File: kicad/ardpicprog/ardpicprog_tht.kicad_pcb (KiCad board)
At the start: 2 copper layers, 69.1 x 53.9 mm, 36 parts, among them P1 CONN_01X06, P2 CONN_01X02, Q1 BC548, SW1 SW_PUSH, U1 PIC16F627, U2 MC34063, U3 LM78L12ACZ

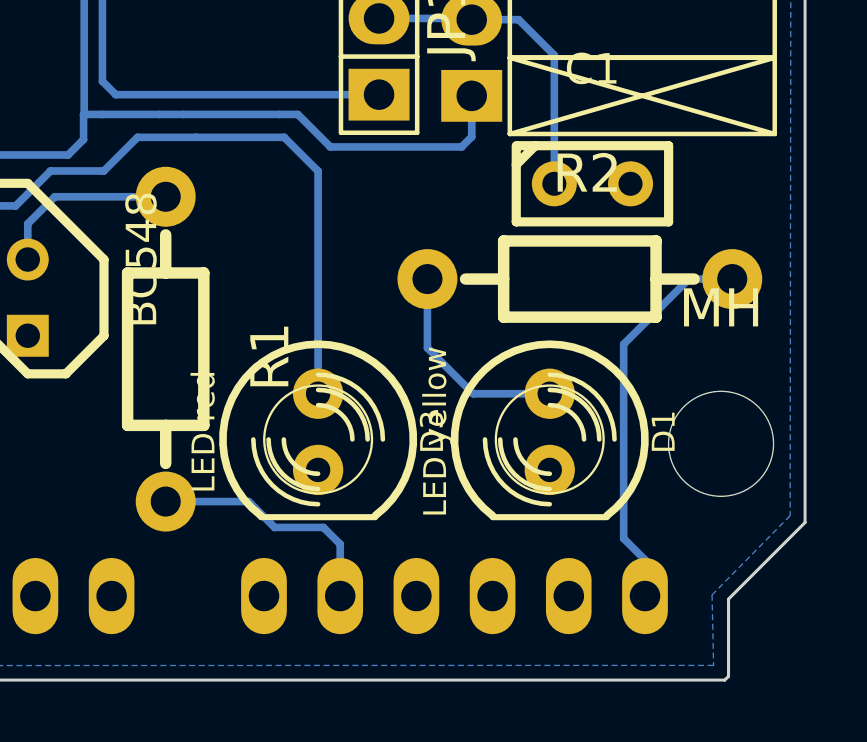
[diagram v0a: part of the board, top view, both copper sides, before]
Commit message: VDD d2 connection fix
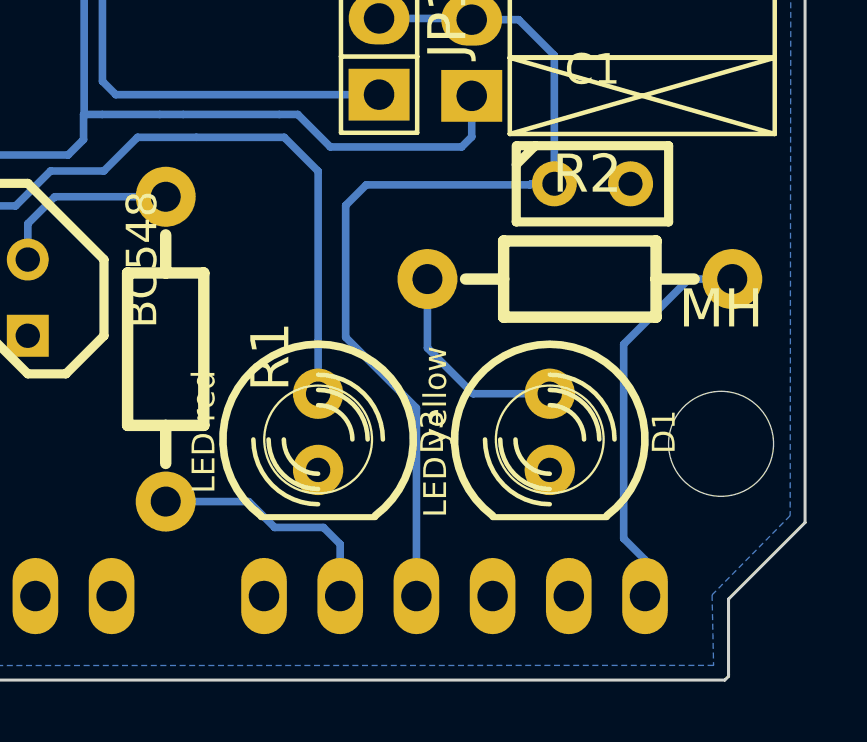
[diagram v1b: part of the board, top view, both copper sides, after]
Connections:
- SHIELD1 pad AD2: (no net) -> VDD(D2)
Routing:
- net VDD(D2): track 10.6 -> 31.9 mm
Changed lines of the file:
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@@
-(kicad_pcb (version 4) (host pcbnew "(2014-jul-16 BZR unknown)-product")
+(kicad_pcb (version 4) (host pcbnew 0.201506232253+5814~23~ubuntu14.04.1-product)
   (general
-    (links 69)
+    (links 70)
     (no_connects 0)
-    (area 76.76617 112.4864 180.28383 175.34946)
+    (area 88.224999 117.774999 157.400001 171.725001)
     (thickness 1.6)
     (drawings 12)
-    (tracks 248)
+    (tracks 255)
     (zones 0)
     (modules 36)
@@
     (pad AD1 thru_hole oval (at 53.34 -2.54 90) (size 2.54 1.524) (drill 1.016) (layers *.Cu *.Mask F.SilkS)
       (net 21 "MCLR(A1)"))
-    (pad AD2 thru_hole oval (at 55.88 -2.54 90) (size 2.54 1.524) (drill 1.016) (layers *.Cu *.Mask F.SilkS))
+    (pad AD2 thru_hole oval (at 55.88 -2.54 90) (size 2.54 1.524) (drill 1.016) (layers *.Cu *.Mask F.SilkS)
+      (net 1 "VDD(D2)"))
     (pad V_IN thru_hole oval (at 45.72 -2.54 90) (size 2.54 1.524) (drill 1.016) (layers *.Cu *.Mask F.SilkS))
     (pad GND2 thru_hole oval (at 43.18 -2.54 90) (size 2.54 1.524) (drill 1.016) (layers *.Cu *.Mask F.SilkS)
@@
   (gr_line (start 153.375 117.825) (end 154.8 119.25) (angle 90) (layer Edge.Cuts) (width 0.1))
   (gr_line (start 153.35 117.825) (end 153.375 117.825) (angle 90) (layer Edge.Cuts) (width 0.1))
+  (segment (start 148.9926 155.133) (end 148.2192 155.133) (width 0.254) (layer B.Cu) (net 1) (status 400000))
+  (segment (start 144.3952 162.607) (end 144.3952 168.8744) (width 0.254) (layer B.Cu) (net 1) (status 800000))
+  (segment (start 142.0368 160.2486) (end 144.3952 162.607) (width 0.254) (layer B.Cu) (net 1))
+  (segment (start 142.0368 155.8544) (end 142.0368 160.2486) (width 0.254) (layer B.Cu) (net 1))
+  (segment (start 142.7226 155.1686) (end 142.0368 155.8544) (width 0.254) (layer B.Cu) (net 1))
+  (segment (start 148.1836 155.1686) (end 142.7226 155.1686) (width 0.254) (layer B.Cu) (net 1))
+  (segment (start 148.2192 155.133) (end 148.1836 155.1686) (width 0.254) (layer B.Cu) (net 1))
   (segment (start 146.23924 149.66184) (end 147.80388 149.66184) (width 0.254) (layer B.Cu) (net 1))
   (segment (start 148.9926 150.85056) (end 148.9926 155.133) (width 0.254) (layer B.Cu) (net 1))

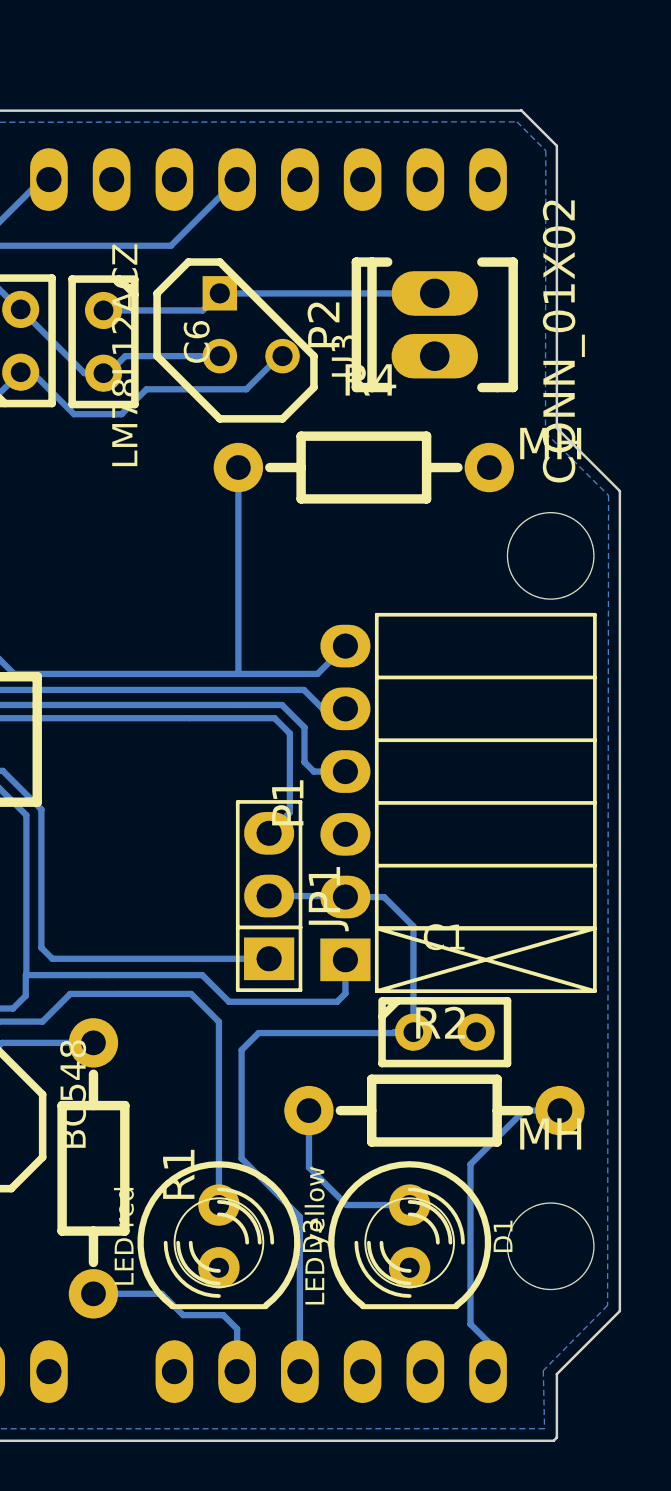
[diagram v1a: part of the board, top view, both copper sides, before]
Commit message: VDD d2 connection fix
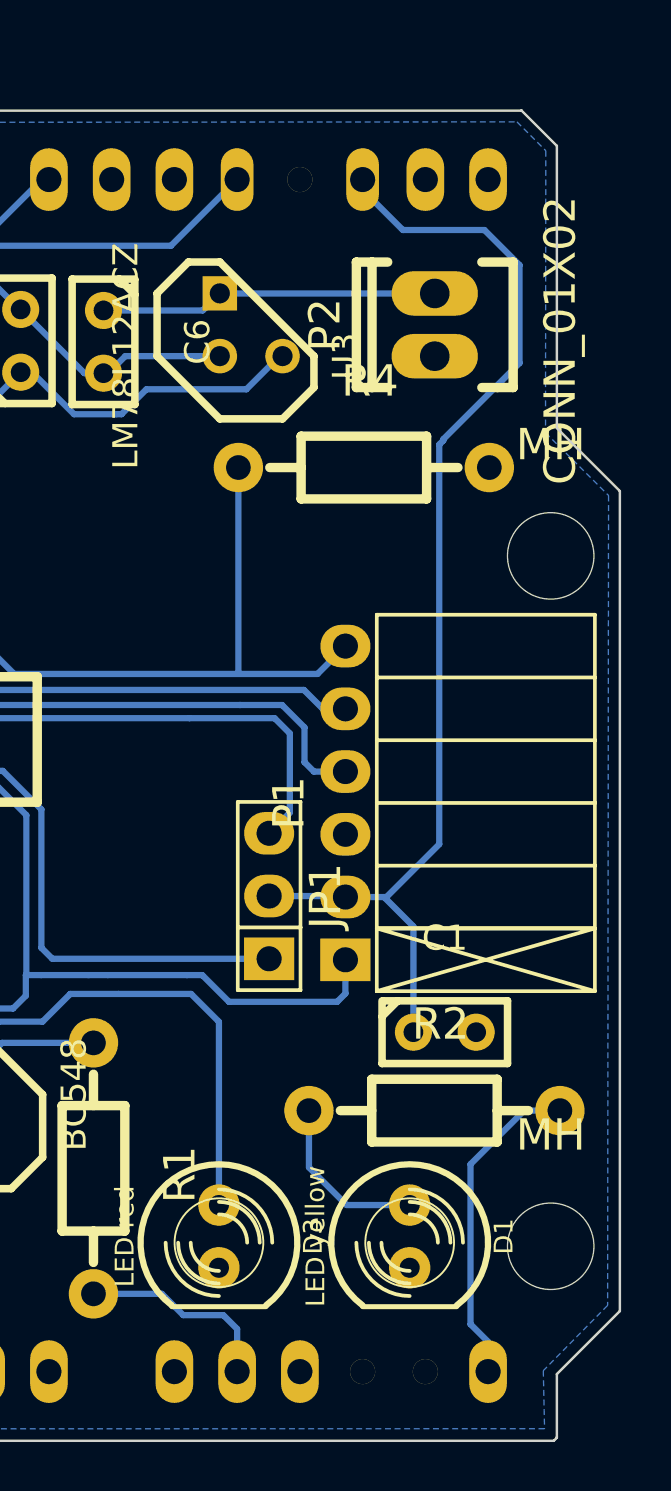
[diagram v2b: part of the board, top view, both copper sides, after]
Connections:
- SHIELD1 pad 2: (no net) -> VDD(D2)
- SHIELD1 pad AD2: VDD(D2) -> (no net)
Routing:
- net VDD(D2): track 31.9 -> 46.6 mm
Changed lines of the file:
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@@
     (links 70)
     (no_connects 0)
-    (area 88.224999 117.774999 157.400001 171.725001)
+    (area 76.76617 112.4864 180.28383 175.34946)
     (thickness 1.6)
     (drawings 12)
-    (tracks 255)
+    (tracks 260)
     (zones 0)
     (modules 36)
@@
     (mod_text_size 1 1)
     (mod_text_width 0.15)
-    (pad_size 1.5 1.5)
-    (pad_drill 0.6)
+    (pad_size 2.54 1.324)
+    (pad_drill 1.016)
     (pad_to_mask_clearance 0)
     (aux_axis_origin 0 0)
@@
     (pad AD5 thru_hole oval (at 63.5 -2.54 90) (size 2.54 1.524) (drill 1.016) (layers *.Cu *.Mask F.SilkS)
       (net 22 "ACTIVITY(A5)"))
-    (pad AD4 thru_hole oval (at 60.96 -2.54 90) (size 2.54 1.524) (drill 1.016) (layers *.Cu *.Mask F.SilkS))
-    (pad AD3 thru_hole oval (at 58.42 -2.54 90) (size 2.54 1.524) (drill 1.016) (layers *.Cu *.Mask F.SilkS))
+    (pad AD4 thru_hole circle (at 60.96 -2.54 90) (size 1.016 1.016) (drill 1.016) (layers *.Cu *.Mask F.SilkS))
+    (pad AD3 thru_hole circle (at 58.42 -2.54 90) (size 1.016 1.016) (drill 1.016) (layers *.Cu *.Mask F.SilkS))
     (pad AD0 thru_hole oval (at 50.8 -2.54 90) (size 2.54 1.524) (drill 1.016) (layers *.Cu *.Mask F.SilkS))
     (pad AD1 thru_hole oval (at 53.34 -2.54 90) (size 2.54 1.524) (drill 1.016) (layers *.Cu *.Mask F.SilkS)
       (net 21 "MCLR(A1)"))
-    (pad AD2 thru_hole oval (at 55.88 -2.54 90) (size 2.54 1.524) (drill 1.016) (layers *.Cu *.Mask F.SilkS)
-      (net 1 "VDD(D2)"))
+    (pad AD2 thru_hole oval (at 55.88 -2.54 90) (size 2.54 1.524) (drill 1.016) (layers *.Cu *.Mask F.SilkS))
     (pad V_IN thru_hole oval (at 45.72 -2.54 90) (size 2.54 1.524) (drill 1.016) (layers *.Cu *.Mask F.SilkS))
     (pad GND2 thru_hole oval (at 43.18 -2.54 90) (size 2.54 1.524) (drill 1.016) (layers *.Cu *.Mask F.SilkS)
@@
     (pad 0 thru_hole oval (at 63.5 -50.8 90) (size 2.54 1.524) (drill 1.016) (layers *.Cu *.Mask F.SilkS))
     (pad 1 thru_hole oval (at 60.96 -50.8 90) (size 2.54 1.524) (drill 1.016) (layers *.Cu *.Mask F.SilkS))
-    (pad 2 thru_hole oval (at 58.42 -50.8 90) (size 2.54 1.524) (drill 1.016) (layers *.Cu *.Mask F.SilkS))
-    (pad 3 thru_hole oval (at 55.88 -50.8 90) (size 2.54 1.524) (drill 1.016) (layers *.Cu *.Mask F.SilkS))
-    (pad 4 thru_hole oval (at 53.34 -50.8 90) (size 2.54 1.524) (drill 1.016) (layers *.Cu *.Mask F.SilkS)
+    (pad 2 thru_hole oval (at 58.42 -50.8 90) (size 2.54 1.324) (drill 1.016) (layers *.Cu *.Mask F.SilkS)
+      (net 1 "VDD(D2)"))
+    (pad 3 thru_hole circle (at 55.88 -50.8 90) (size 1.016 1.016) (drill 1.016) (layers *.Cu *.Mask F.SilkS))
+    (pad 4 thru_hole oval (at 53.34 -50.8 90) (size 2.54 1.324) (drill 1.016) (layers *.Cu *.Mask F.SilkS)
       (net 18 "CLK(D4)"))
     (pad 5 thru_hole oval (at 50.8 -50.8 90) (size 2.54 1.524) (drill 1.016) (layers *.Cu *.Mask F.SilkS))
@@
   (gr_line (start 153.375 117.825) (end 154.8 119.25) (angle 90) (layer Edge.Cuts) (width 0.1))
   (gr_line (start 153.35 117.825) (end 153.375 117.825) (angle 90) (layer Edge.Cuts) (width 0.1))
-  (segment (start 148.9926 155.133) (end 148.2192 155.133) (width 0.254) (layer B.Cu) (net 1) (status 400000))
-  (segment (start 144.3952 162.607) (end 144.3952 168.8744) (width 0.254) (layer B.Cu) (net 1) (status 800000))
-  (segment (start 142.0368 160.2486) (end 144.3952 162.607) (width 0.254) (layer B.Cu) (net 1))
-  (segment (start 142.0368 155.8544) (end 142.0368 160.2486) (width 0.254) (layer B.Cu) (net 1))
-  (segment (start 142.7226 155.1686) (end 142.0368 155.8544) (width 0.254) (layer B.Cu) (net 1))
-  (segment (start 148.1836 155.1686) (end 142.7226 155.1686) (width 0.254) (layer B.Cu) (net 1))
-  (segment (start 148.2192 155.133) (end 148.1836 155.1686) (width 0.254) (layer B.Cu) (net 1))
-  (segment (start 146.23924 149.66184) (end 147.80388 149.66184) (width 0.254) (layer B.Cu) (net 1))
+  (segment (start 150.2029 131.1783) (end 150.2029 131.1275) (width 0.254) (layer B.Cu) (net 1))
+  (segment (start 153.289 124.079) (end 151.8666 122.6566) (width 0.254) (layer B.Cu) (net 1))
+  (segment (start 153.289 128.0414) (end 153.289 124.079) (width 0.254) (layer B.Cu) (net 1))
+  (segment (start 150.2029 131.1275) (end 153.289 128.0414) (width 0.254) (layer B.Cu) (net 1))
+  (segment (start 150.0378 131.3434) (end 150.0378 147.5232) (width 0.254) (layer B.Cu) (net 1))
+  (segment (start 150.2029 131.1783) (end 150.0378 131.3434) (width 0.254) (layer B.Cu) (net 1))
+  (segment (start 146.9352 120.6144) (end 146.9352 121.0272) (width 0.254) (layer B.Cu) (net 1))
+  (segment (start 146.9352 121.0272) (end 148.5646 122.6566) (width 0.254) (layer B.Cu) (net 1))
+  (segment (start 148.5646 122.6566) (end 151.8666 122.6566) (width 0.254) (layer B.Cu) (net 1))
+  (segment (start 147.8026 149.66184) (end 147.89916 149.66184) (width 0.254) (layer B.Cu) (net 1))
+  (segment (start 147.89916 149.66184) (end 150.0378 147.5232) (width 0.254) (layer B.Cu) (net 1))
+  (segment (start 146.23924 149.66184) (end 147.8026 149.66184) (width 0.254) (layer B.Cu) (net 1))
+  (segment (start 147.8026 149.66184) (end 147.80388 149.66184) (width 0.254) (layer B.Cu) (net 1))
   (segment (start 148.9926 150.85056) (end 148.9926 155.133) (width 0.254) (layer B.Cu) (net 1))
   (segment (start 147.80388 149.66184) (end 148.9926 150.85056) (width 0.254) (layer B.Cu) (net 1))
